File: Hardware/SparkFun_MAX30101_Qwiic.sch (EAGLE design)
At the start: 44 parts, among them J1 PTH, J3 QWIIC_RA, J5 QWIIC_RA, Q6 20V/0.2A/8MHz/1.2Ω/1Vth, Q8 20V/0.2A/8MHz/1.2Ω/1Vth, U1 1.8V/100mA, U2 MAX30101EFD, U3 PAM2401

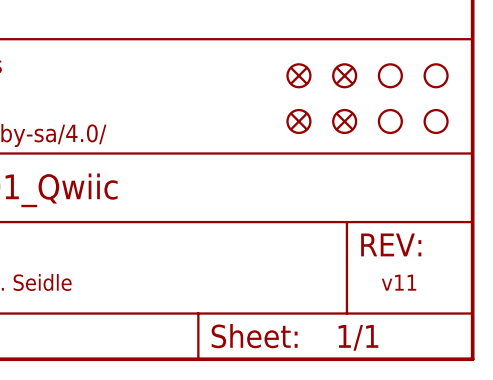
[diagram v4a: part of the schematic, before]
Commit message: Updated name silk to "Photodetector"
Also bumped version to v12 on sch and brd
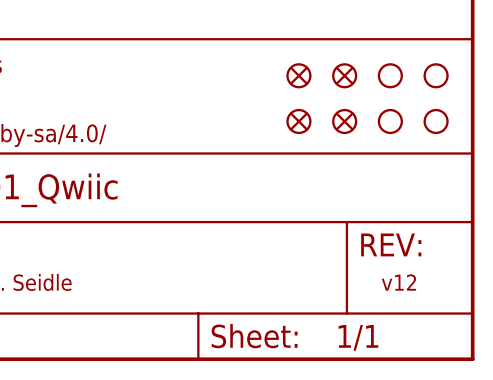
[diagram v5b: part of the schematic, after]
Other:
- note added: "v12"
- note removed: "v11"
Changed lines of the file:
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@@
 <grid distance="0.1" unitdist="inch" unit="inch" style="lines" multiple="1" display="no" altdistance="0.01" altunitdist="inch" altunit="inch"/>
 <layers>
-<layer number="1" name="Top" color="4" fill="1" visible="yes" active="no"/>
-<layer number="2" name="Route2" color="1" fill="3" visible="yes" active="no"/>
-<layer number="3" name="Route3" color="4" fill="3" visible="yes" active="no"/>
-<layer number="4" name="Route4" color="1" fill="4" visible="yes" active="no"/>
-<layer number="5" name="Route5" color="4" fill="4" visible="yes" active="no"/>
-<layer number="6" name="Route6" color="1" fill="8" visible="yes" active="no"/>
-<layer number="7" name="Route7" color="4" fill="8" visible="yes" active="no"/>
-<layer number="8" name="Route8" color="1" fill="2" visible="yes" active="no"/>
-<layer number="9" name="Route9" color="4" fill="2" visible="yes" active="no"/>
-<layer number="10" name="Route10" color="1" fill="7" visible="yes" active="no"/>
-<layer number="11" name="Route11" color="4" fill="7" visible="yes" active="no"/>
-<layer number="12" name="Route12" color="1" fill="5" visible="yes" active="no"/>
-<layer number="13" name="Route13" color="4" fill="5" visible="yes" active="no"/>
-<layer number="14" name="Route14" color="1" fill="6" visible="yes" active="no"/>
-<layer number="15" name="Route15" color="4" fill="6" visible="yes" active="no"/>
-<layer number="16" name="Bottom" color="1" fill="1" visible="yes" active="no"/>
-<layer number="17" name="Pads" color="2" fill="1" visible="yes" active="no"/>
-<layer number="18" name="Vias" color="2" fill="1" visible="yes" active="no"/>
-<layer number="19" name="Unrouted" color="6" fill="1" visible="yes" active="no"/>
-<layer number="20" name="Dimension" color="15" fill="1" visible="yes" active="no"/>
-<layer number="21" name="tPlace" color="16" fill="1" visible="yes" active="no"/>
-<layer number="22" name="bPlace" color="14" fill="1" visible="yes" active="no"/>
-<layer number="23" name="tOrigins" color="15" fill="1" visible="yes" active="no"/>
-<layer number="24" name="bOrigins" color="15" fill="1" visible="yes" active="no"/>
-<layer number="25" name="tNames" color="7" fill="1" visible="yes" active="no"/>
-<layer number="26" name="bNames" color="7" fill="1" visible="yes" active="no"/>
-<layer number="27" name="tValues" color="7" fill="1" visible="yes" active="no"/>
-<layer number="28" name="bValues" color="7" fill="1" visible="yes" active="no"/>
+<layer number="1" name="Top" color="4" fill="1" visible="no" active="no"/>
+<layer number="2" name="Route2" color="1" fill="3" visible="no" active="no"/>
+<layer number="3" name="Route3" color="4" fill="3" visible="no" active="no"/>
+<layer number="4" name="Route4" color="1" fill="4" visible="no" active="no"/>
+<layer number="5" name="Route5" color="4" fill="4" visible="no" active="no"/>
+<layer number="6" name="Route6" color="1" fill="8" visible="no" active="no"/>
+<layer number="7" name="Route7" color="4" fill="8" visible="no" active="no"/>
+<layer number="8" name="Route8" color="1" fill="2" visible="no" active="no"/>
+<layer number="9" name="Route9" color="4" fill="2" visible="no" active="no"/>
+<layer number="10" name="Route10" color="1" fill="7" visible="no" active="no"/>
+<layer number="11" name="Route11" color="4" fill="7" visible="no" active="no"/>
+<layer number="12" name="Route12" color="1" fill="5" visible="no" active="no"/>
+<layer number="13" name="Route13" color="4" fill="5" visible="no" active="no"/>
+<layer number="14" name="Route14" color="1" fill="6" visible="no" active="no"/>
+<layer number="15" name="Route15" color="4" fill="6" visible="no" active="no"/>
+<layer number="16" name="Bottom" color="1" fill="1" visible="no" active="no"/>
+<layer number="17" name="Pads" color="2" fill="1" visible="no" active="no"/>
+<layer number="18" name="Vias" color="2" fill="1" visible="no" active="no"/>
+<layer number="19" name="Unrouted" color="6" fill="1" visible="no" active="no"/>
+<layer number="20" name="Dimension" color="15" fill="1" visible="no" active="no"/>
+<layer number="21" name="tPlace" color="16" fill="1" visible="no" active="no"/>
+<layer number="22" name="bPlace" color="14" fill="1" visible="no" active="no"/>
+<layer number="23" name="tOrigins" color="15" fill="1" visible="no" active="no"/>
+<layer number="24" name="bOrigins" color="15" fill="1" visible="no" active="no"/>
+<layer number="25" name="tNames" color="7" fill="1" visible="no" active="no"/>
+<layer number="26" name="bNames" color="7" fill="1" visible="no" active="no"/>
+<layer number="27" name="tValues" color="7" fill="1" visible="no" active="no"/>
+<layer number="28" name="bValues" color="7" fill="1" visible="no" active="no"/>
 <layer number="29" name="tStop" color="5" fill="5" visible="no" active="no"/>
 <layer number="30" name="bStop" color="7" fill="6" visible="no" active="no"/>
@@
 <layer number="35" name="tGlue" color="7" fill="4" visible="no" active="no"/>
 <layer number="36" name="bGlue" color="7" fill="5" visible="no" active="no"/>
-<layer number="37" name="tTest" color="7" fill="1" visible="yes" active="no"/>
-<layer number="38" name="bTest" color="7" fill="1" visible="yes" active="no"/>
+<layer number="37" name="tTest" color="7" fill="1" visible="no" active="no"/>
+<layer number="38" name="bTest" color="7" fill="1" visible="no" active="no"/>
 <layer number="39" name="tKeepout" color="4" fill="11" visible="no" active="no"/>
 <layer number="40" name="bKeepout" color="1" fill="11" visible="no" active="no"/>
@@
 <layer number="44" name="Drills" color="7" fill="1" visible="no" active="no"/>
 <layer number="45" name="Holes" color="7" fill="1" visible="no" active="no"/>
-<layer number="46" name="Milling" color="3" fill="1" visible="yes" active="no"/>
-<layer number="47" name="Measures" color="7" fill="1" visible="yes" active="no"/>
-<layer number="48" name="Document" color="7" fill="1" visible="yes" active="no"/>
-<layer number="49" name="Reference" color="7" fill="1" visible="yes" active="no"/>
-<layer number="50" name="dxf" color="7" fill="1" visible="yes" active="no"/>
-<layer number="51" name="tDocu" color="6" fill="1" visible="yes" active="no"/>
-<layer number="52" name="bDocu" color="7" fill="1" visible="yes" active="no"/>
-<layer number="53" name="tGND_GNDA" color="7" fill="9" visible="yes" active="no"/>
-<layer number="54" name="bGND_GNDA" color="1" fill="9" visible="yes" active="no"/>
-<layer number="56" name="wert" color="7" fill="1" visible="yes" active="no"/>
-<layer number="57" name="tCAD" color="7" fill="1" visible="yes" active="no"/>
-<layer number="59" name="tCarbon" color="7" fill="1" visible="yes" active="no"/>
-<layer number="60" name="bCarbon" color="7" fill="1" visible="yes" active="no"/>
+<layer number="46" name="Milling" color="3" fill="1" visible="no" active="no"/>
+<layer number="47" name="Measures" color="7" fill="1" visible="no" active="no"/>
+<layer number="48" name="Document" color="7" fill="1" visible="no" active="no"/>
+<layer number="49" name="Reference" color="7" fill="1" visible="no" active="no"/>
+<layer number="50" name="dxf" color="7" fill="1" visible="no" active="no"/>
+<layer number="51" name="tDocu" color="6" fill="1" visible="no" active="no"/>
+<layer number="52" name="bDocu" color="7" fill="1" visible="no" active="no"/>
+<layer number="53" name="tGND_GNDA" color="7" fill="9" visible="no" active="no"/>
+<layer number="54" name="bGND_GNDA" color="1" fill="9" visible="no" active="no"/>
+<layer number="56" name="wert" color="7" fill="1" visible="no" active="no"/>
+<layer number="57" name="tCAD" color="7" fill="1" visible="no" active="no"/>
+<layer number="59" name="tCarbon" color="7" fill="1" visible="no" active="no"/>
+<layer number="60" name="bCarbon" color="7" fill="1" visible="no" active="no"/>
 <layer number="88" name="SimResults" color="9" fill="1" visible="yes" active="yes"/>
 <layer number="89" name="SimProbes" color="9" fill="1" visible="yes" active="yes"/>
@@
 <plain>
 <text x="111.76" y="60.96" size="2.54" layer="97" font="vector">7-Bit I2C: 0x57</text>
-<text x="238.76" y="7.62" size="1.778" layer="94" font="vector">v11</text>
+<text x="238.76" y="7.62" size="1.778" layer="94" font="vector">v12</text>
 <text x="170.688" y="11.43" size="2.54" layer="94" font="vector">Pete Lewis</text>
 <wire x1="106.68" y1="185.42" x2="106.68" y2="127" width="0.2032" layer="97" style="longdash"/>
